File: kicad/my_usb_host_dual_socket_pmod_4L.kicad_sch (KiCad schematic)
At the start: 16 parts, among them IC1 TPS61253AYFFR, J1 UK-USB AF 90-19.6, J2 Conn_02x06_Odd_Even, J3 Conn_01x02_Socket

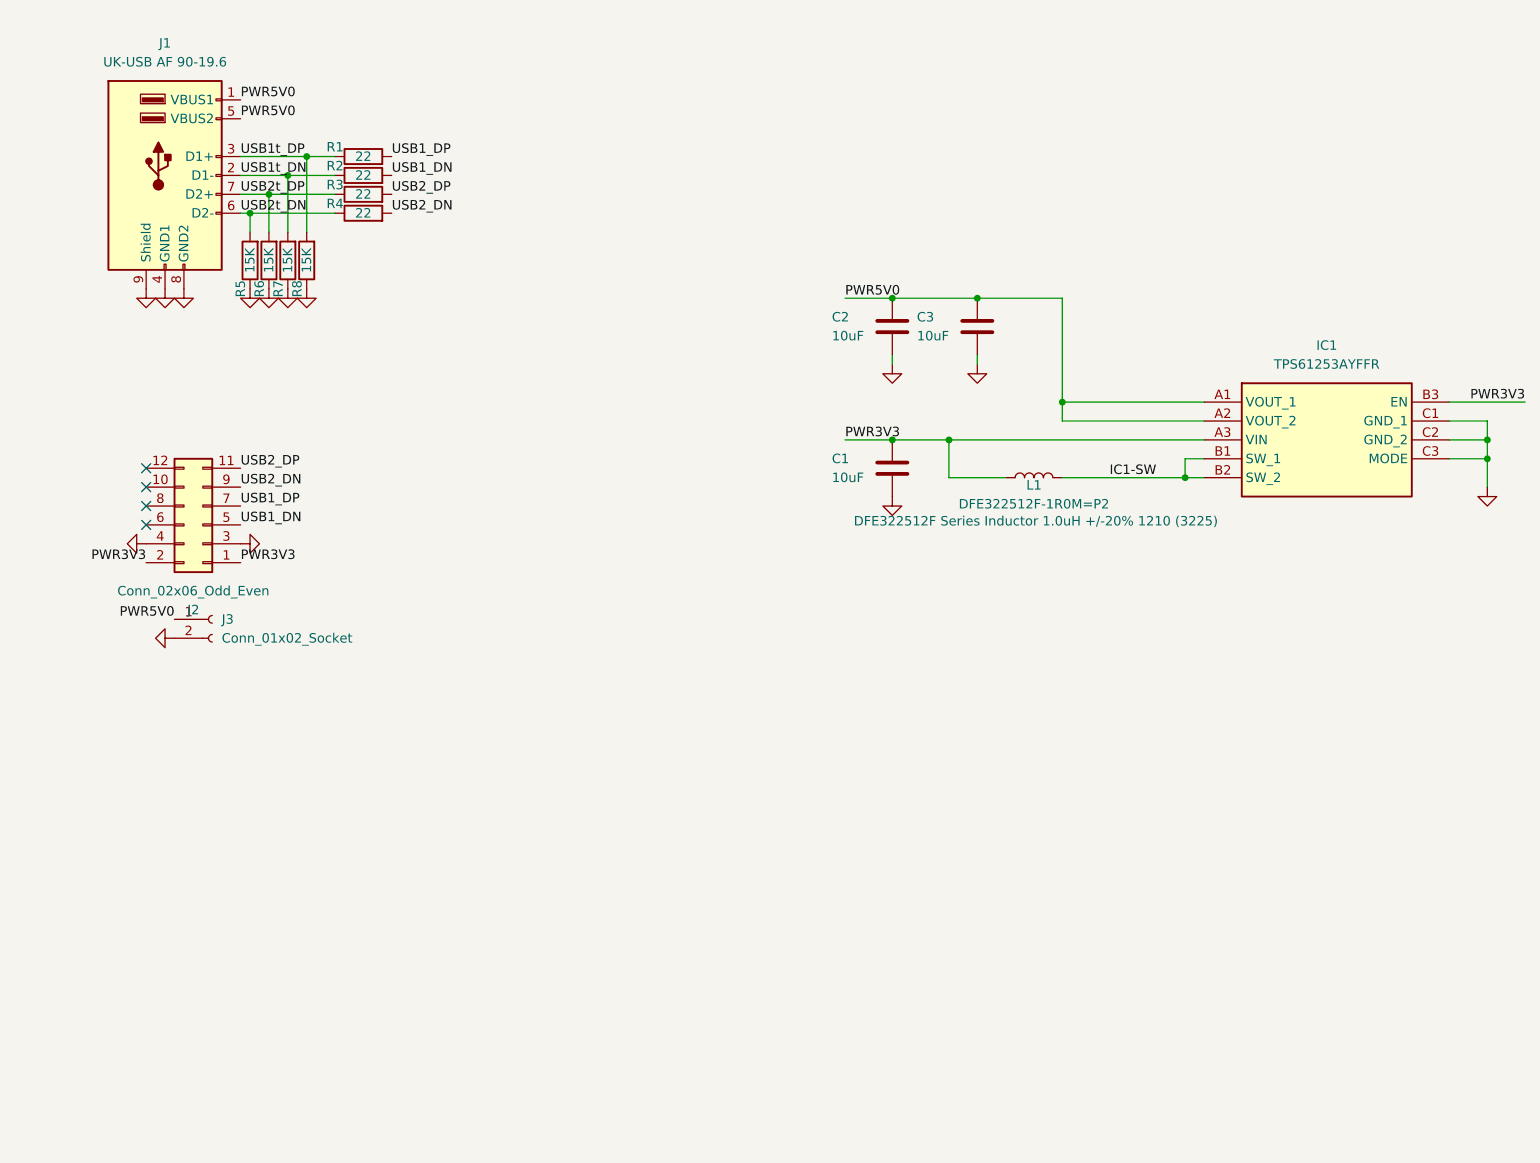
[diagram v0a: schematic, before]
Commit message: Changed to 4-layer stackup for matched USB 50/90 impedance and added ESD protection
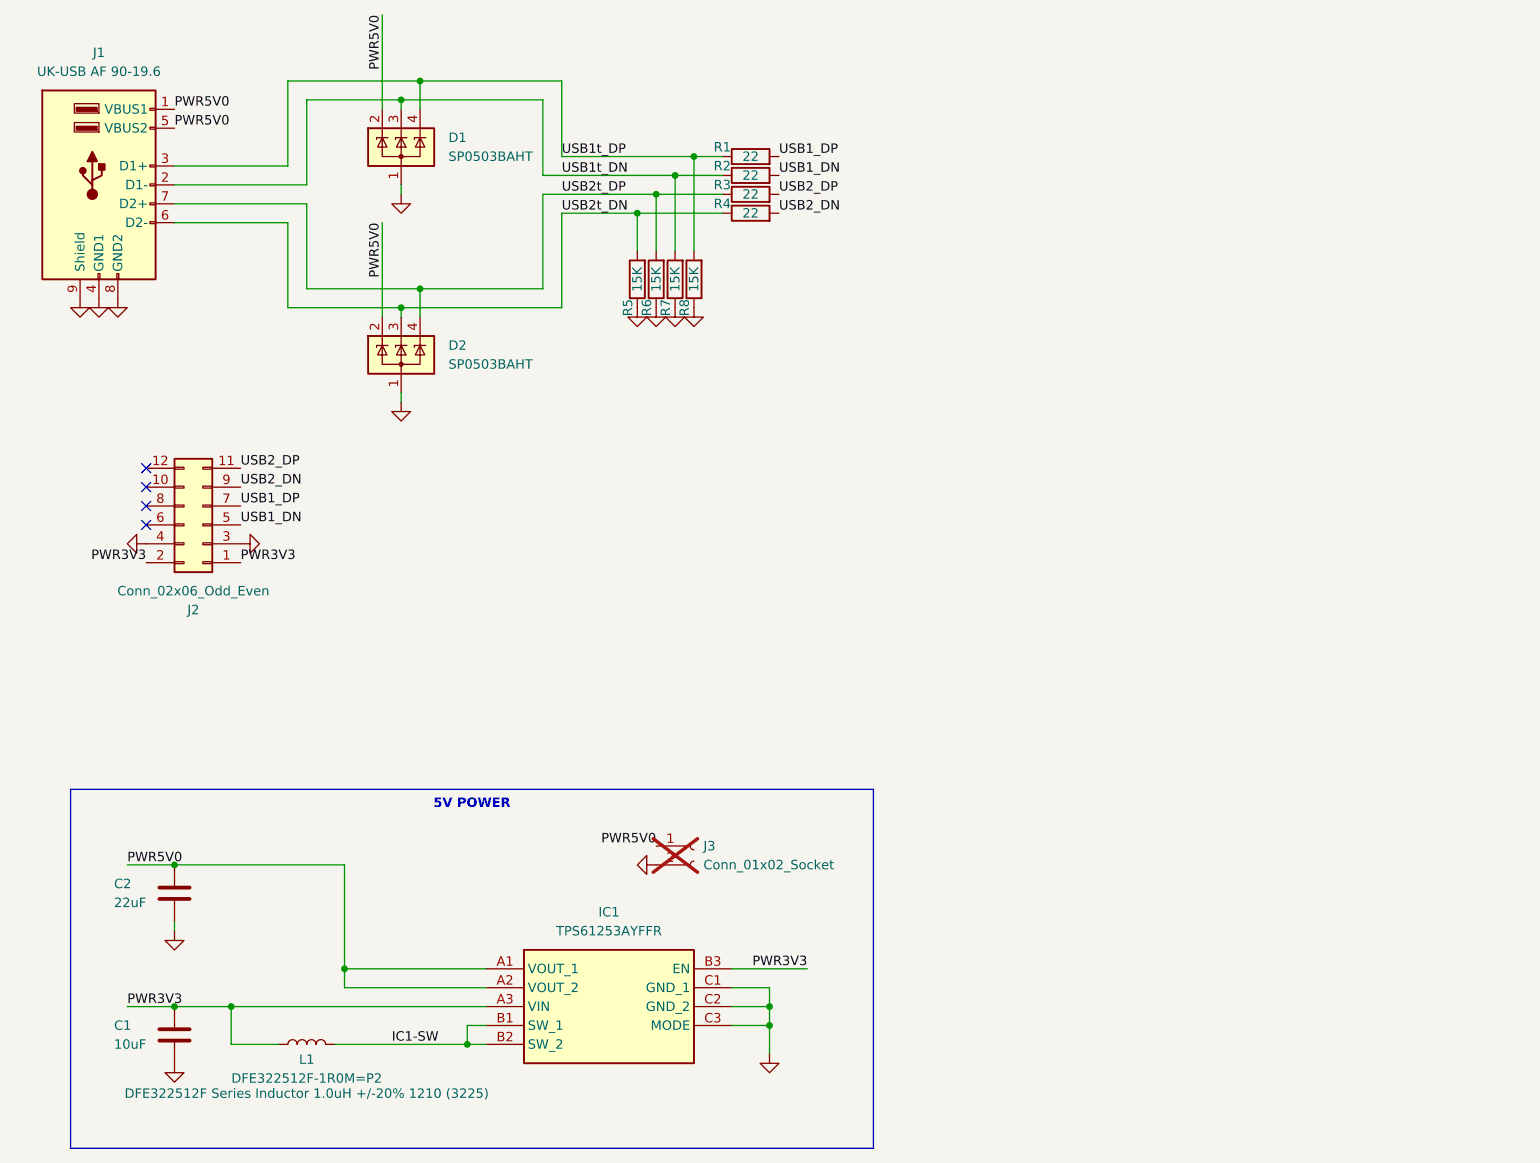
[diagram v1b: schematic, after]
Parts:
- removed C3: 10uF, Capacitor_SMD:C_0603_1608Metric, symbol Device:C
- added D1, D2: SP0503BAHT, Package_TO_SOT_SMD:SOT-143, symbol Power_Protection:SP0503BAHT
- C1: footprint Capacitor_SMD:C_0402_1005Metric -> Capacitor_SMD:C_0603_1608Metric
- C2: value 10uF -> 22uF; footprint Capacitor_SMD:C_0603_1608Metric -> Capacitor_SMD:C_1206_3216Metric
- IC1: footprint libs:BGA9C40P3X3_119X129X62 -> usb_host_pmod:BGA9C40P3X3_119X129X62
- J1: footprint Connector_USB:USB_A_Wuerth_61400826021_Horizontal_Stacked -> usb_host_pmod:USB_A_Wuerth_61400826021_Horizontal_Stacked
- J3: now not fitted
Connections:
- net GND: now also D1.1 (A), D2.1 (A)
- net PWR5V0: now also D1.2 (K), D2.2 (K)
- net USB1t_DN: now also D1.3 (K)
- net USB1t_DP: now also D1.4 (K)
- net USB2t_DN: now also D2.3 (K)
- net USB2t_DP: now also D2.4 (K)
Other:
- moved on the sheet: C1, C2, IC1, J1, L1, R1, R2, R3, R4, R5, R6, R7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
